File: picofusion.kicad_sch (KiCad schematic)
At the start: 48 parts, among them J1 NORTH, J2 EAST, J3 WEST, J4 SOUTH, U1 W25Q16, U2 RP2040, U3 TLV71333PDQN, U7 TJA1051TK-3, Y1 12MHz

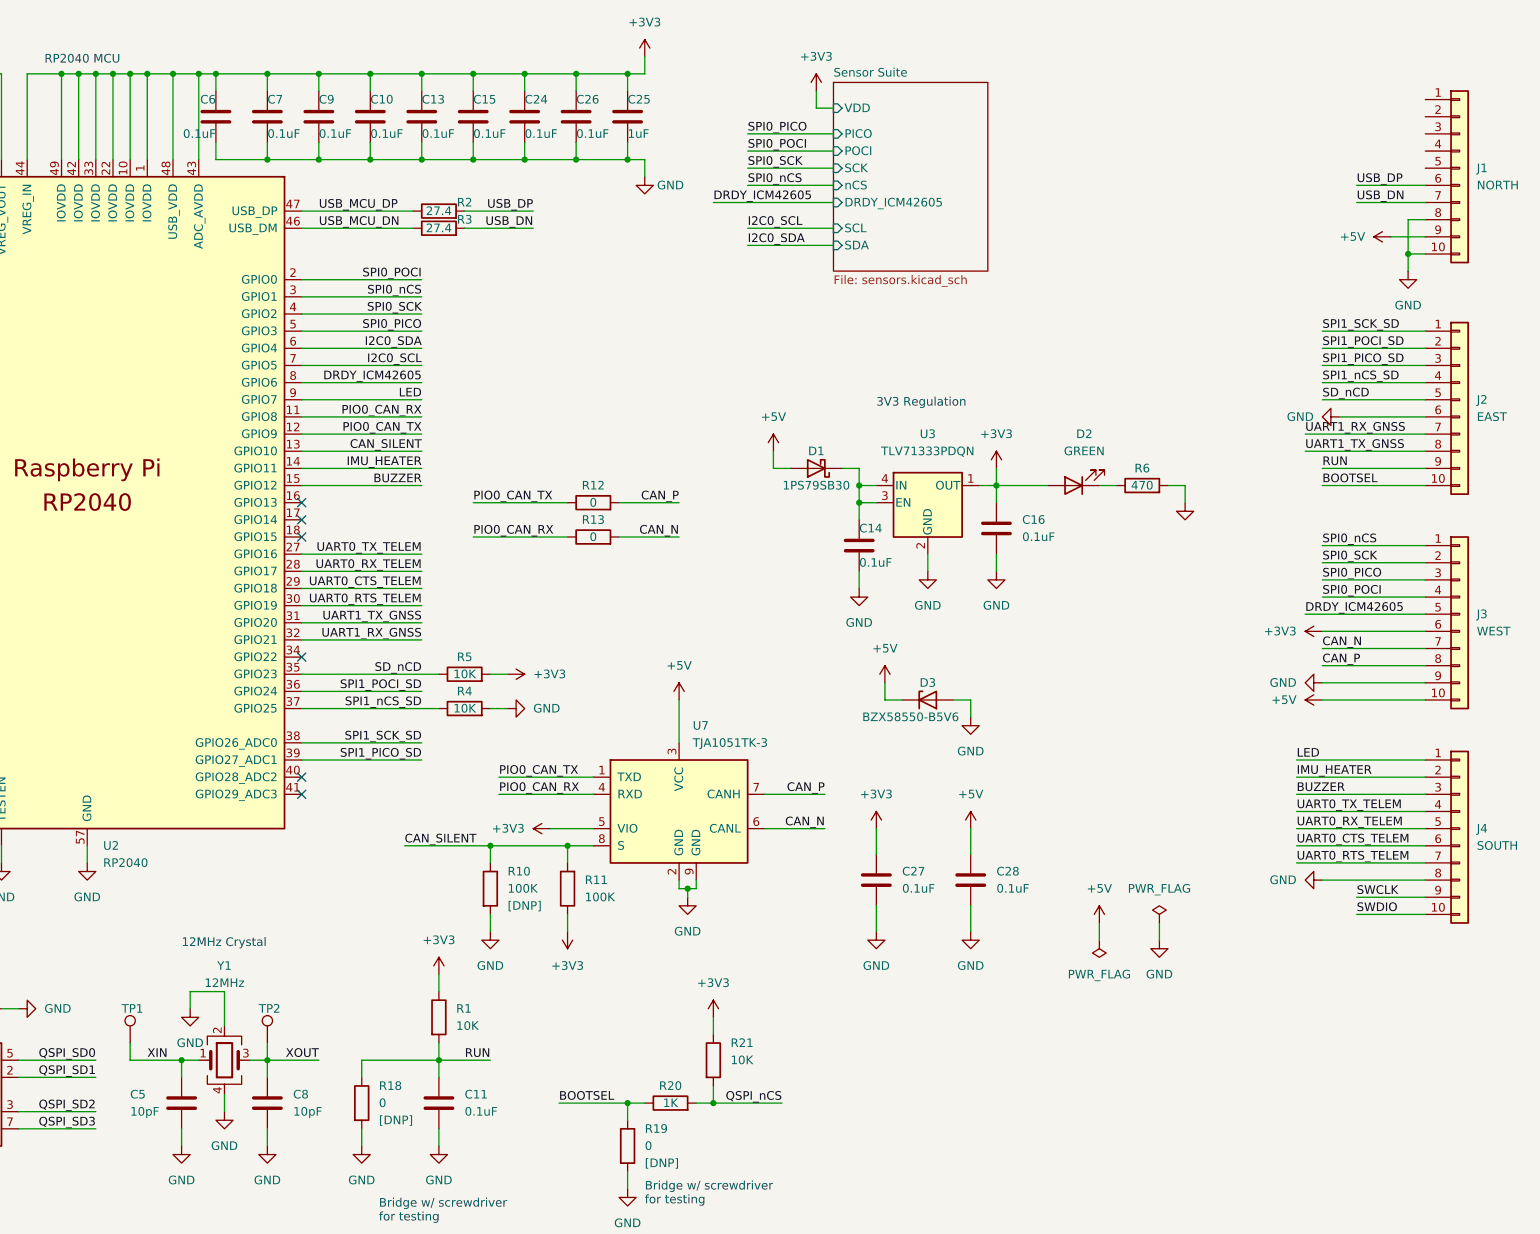
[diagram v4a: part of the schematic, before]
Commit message: h10: add graphics, fix drc, minor modifications
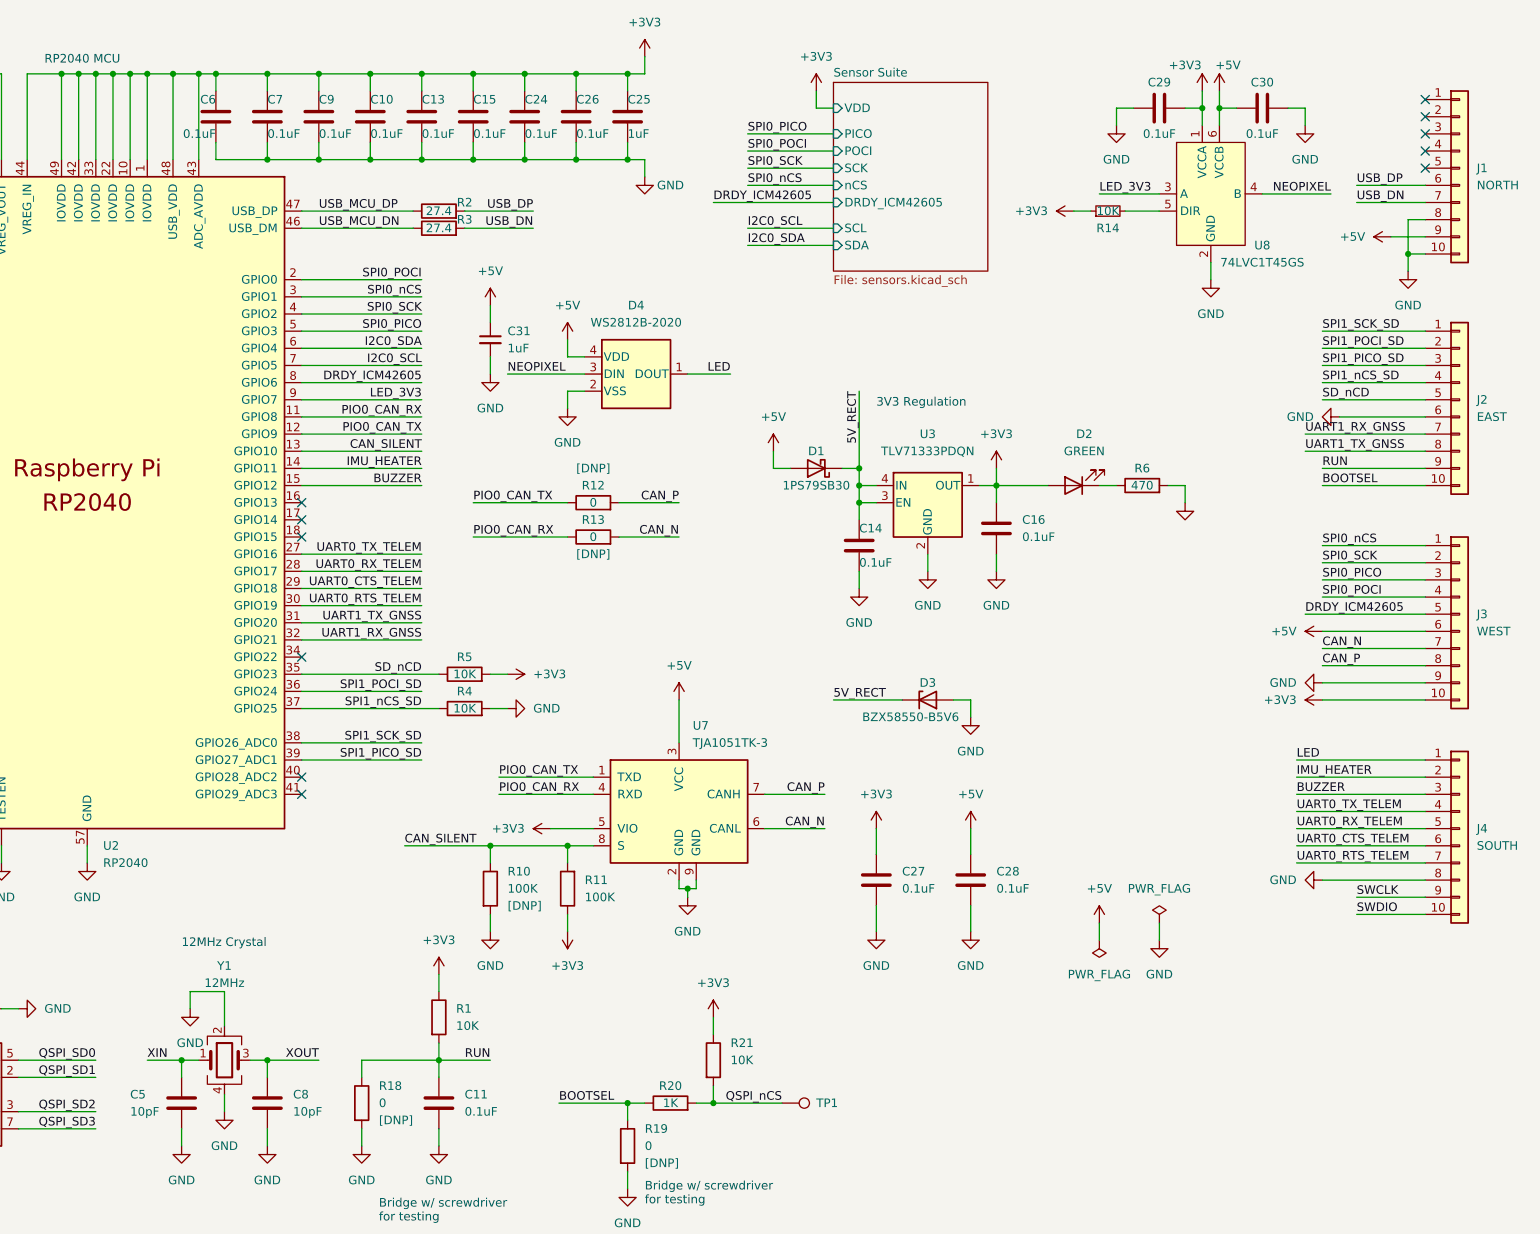
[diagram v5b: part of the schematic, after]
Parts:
- removed TP2: TestPoint, TestPoint:TestPoint_Pad_D1.0mm, symbol Connector:TestPoint
- added C29, C30: 0.1uF, Capacitor_SMD:C_0201_0603Metric, symbol Device:C
- added C31: 1uF, Capacitor_SMD:C_0201_0603Metric, symbol Device:C_Small
- added D4: WS2812B-2020, LED_SMD_Extra:WS2812B-2020, symbol LED_Extra:WS2812B-2020
- added R14: 10K, Resistor_SMD:R_0402_1005Metric, symbol Device:R_Small
- added U8: 74LVC1T45GS, 74LVC1T45:PSON35P100X100X35-6N, symbol 74LVC1T45:74LVC1T45GS
- J1, J2, J3, J4: footprint Connector_PinHeader_2.00mm:PinHeader_1x10_P2.00mm_Vertical -> picofusion_stamp:PinCastellation_1x10_P2.00mm_Vertical
- R12, R13: DNP (none) -> [DNP]
- TP1: footprint TestPoint:TestPoint_Pad_D1.0mm -> TestPoint:TestPoint_Pad_1.0x1.0mm
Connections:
- net +3V3: now also J3.10 (Pin_10), C29.2, R14.1, U8.1 (VCCA); no longer J3.6 (Pin_6)
- net +5V: now also J3.6 (Pin_6), C30.2, C31.1, D4.4 (VDD), U8.6 (VCCB); no longer D3.1 (K), J3.10 (Pin_10)
- net GND: now also C29.1, C30.1, C31.2, D4.2 (VSS), U8.2 (GND)
- net LED: now also D4.1 (DOUT); no longer U2.9 (GPIO7)
- net QSPI_nCS: now also TP1.1
- net XIN: no longer TP1.1
- net 5V_RECT: now reaches C14.1, D1.1 (K), U3.3 (EN), U3.4 (IN)
- net 5V_RECT: now also D3.1 (K)
- new net: R14.2, U8.5 (DIR)
- new net LED_3V3: U2.9 (GPIO7), U8.3 (A)
- new net NEOPIXEL: D4.3 (DIN), U8.4 (B)
- no-connect marks 6 -> 11

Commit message: h10: r2 final
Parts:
- added R15, R16, R17, R22: 22K, Resistor_SMD:R_0201_0603Metric, symbol Device:R
- C1, C10, C11, C13, C15, C2, C24, C26, C27, C28, C4, C6, C7, C9: LCSC C1525 -> (none); Mfr. # CC0201KRX5R5BB104 -> (none)
- C14, C16: LCSC C1525 -> (none)
- C25, C3: LCSC C52923 -> (none)
- C5, C8: LCSC C1547 -> (none)
- D1: LCSC C426690 -> (none)
- D2: LCSC C72043 -> (none); Part (none) -> QBLP595-IG
- J1, J2, J3, J4, TP1: now left out of the parts list
- R1, R21, R4, R5: LCSC C25744 -> (none)
- R10, R11: LCSC C25741 -> (none)
- R12, R13: LCSC C17168 -> (none)
- R2, R3: value 27.4 -> 27; LCSC C31439 -> (none)
- R6: LCSC C25117 -> (none)
- U1: LCSC C2843335 -> (none)
- U2: LCSC C2040 -> (none)
- U3: LCSC C2866431 -> (none)
- U7: LCSC C124020 -> (none)
- Y1: LCSC C521567 -> (none); Part (none) -> R2520-12.000-10-3030-TR
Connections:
- net +3V3: now also R17.1
- net +5V: now also R15.1
- net GND: now also R16.2, R22.2
- net I2C0_SCL: now also J1.4 (Pin_4)
- net I2C0_SDA: now also J1.5 (Pin_5)
- net RESV1: now reaches U2.16 (GPIO13)
- net RESV1: now also J1.3 (Pin_3)
- net 3V3_SENSE: now reaches U2.40 (GPIO28_ADC2)
- net 3V3_SENSE: now also R17.2, R22.1
- net 5V_SENSE: now reaches U2.41 (GPIO29_ADC3)
- net 5V_SENSE: now also R15.2, R16.1
- no-connect marks 11 -> 5
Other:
- moved on the sheet: C27, C28

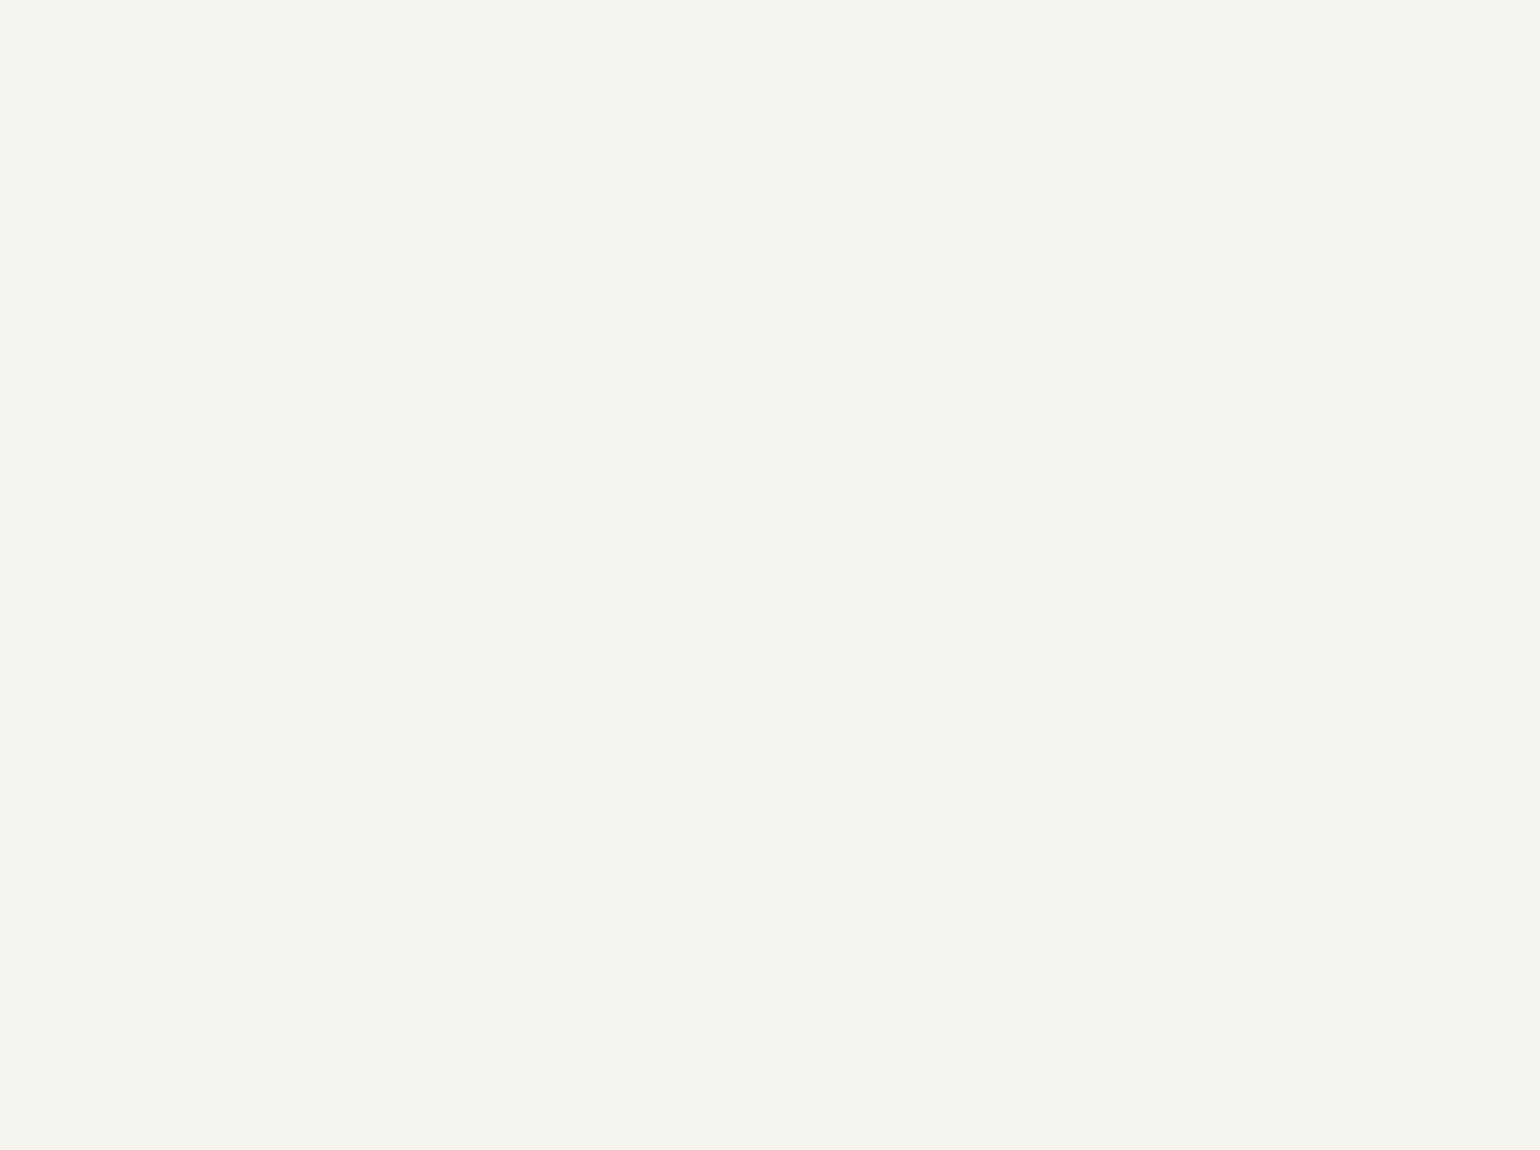
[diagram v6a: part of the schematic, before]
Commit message: added f412 and did test routing
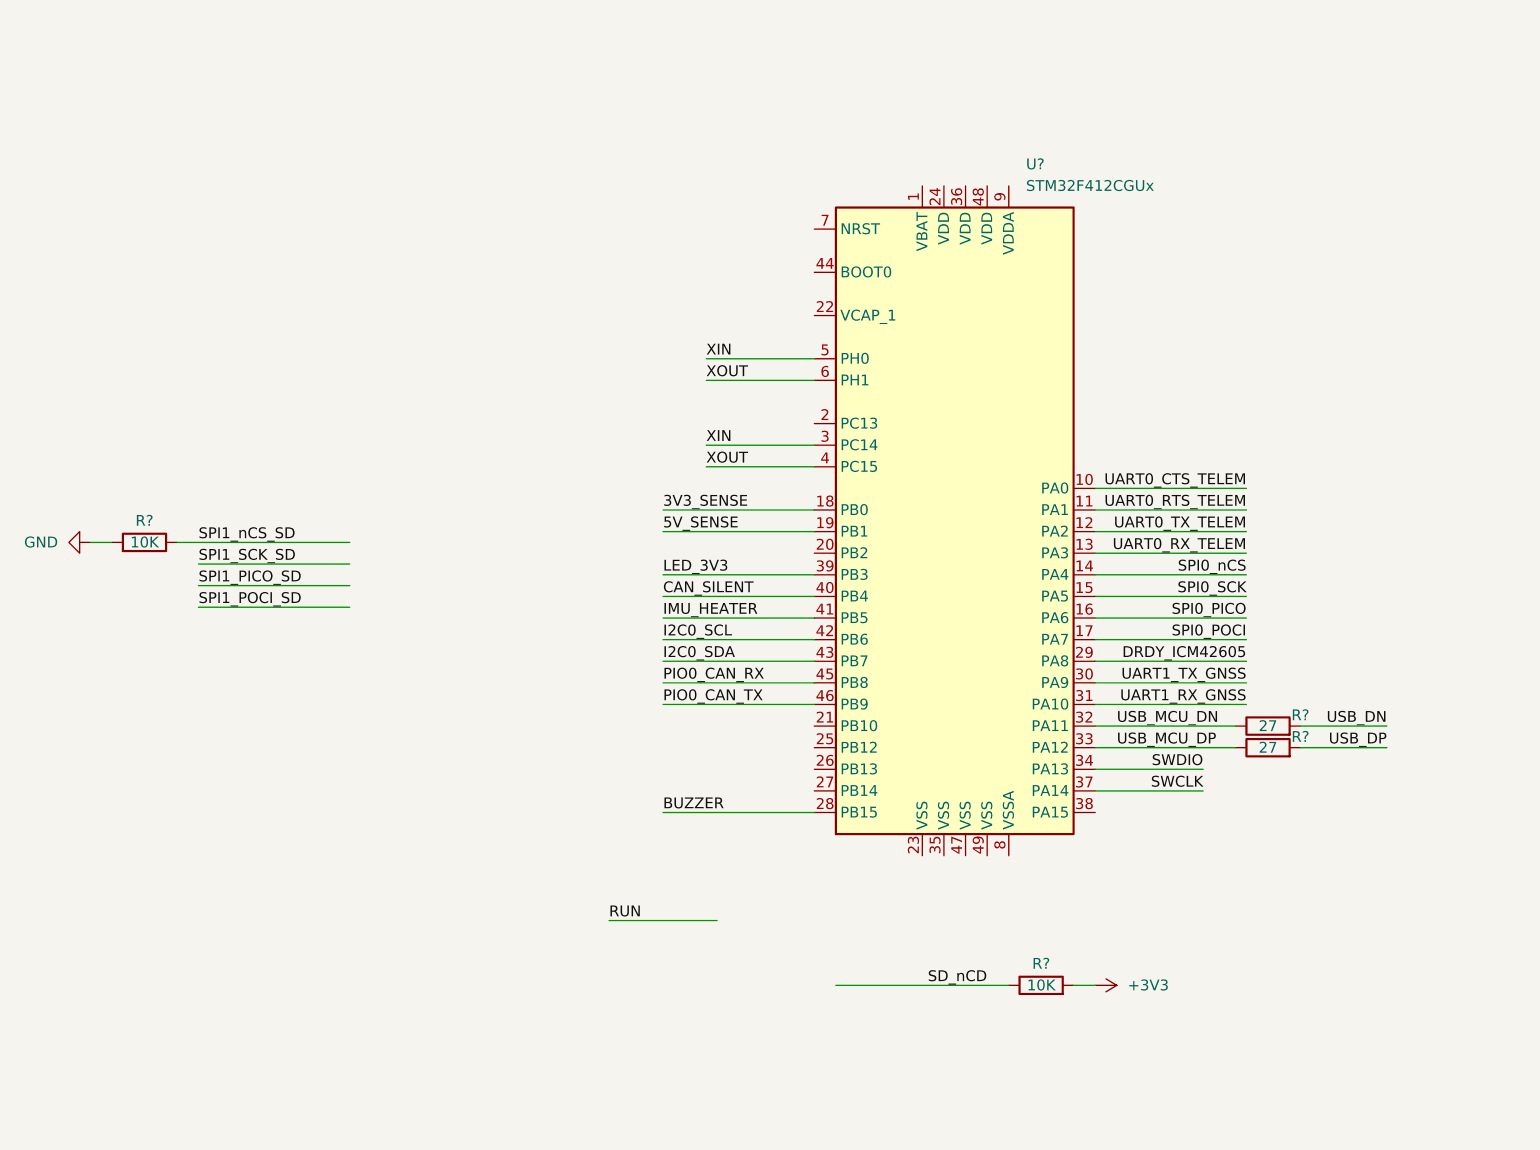
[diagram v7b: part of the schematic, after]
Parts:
- added R? (x2): 27, Resistor_SMD:R_0201_0603Metric, symbol Device:R
- added R? (x2): 10K, Resistor_SMD:R_0402_1005Metric, symbol Device:R
- added U?: STM32F412CGUx, Package_DFN_QFN:QFN-48-1EP_7x7mm_P0.5mm_EP5.6x5.6mm, symbol MCU_ST_STM32F4:STM32F412CGUx
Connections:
- net +3V3: now also R?.2
- net 3V3_SENSE: now also U?.18 (PB0)
- net 5V_SENSE: now also U?.19 (PB1)
- net BUZZER: now also U?.28 (PB15)
- net CAN_SILENT: now also U?.40 (PB4)
- net DRDY_ICM42605: now also U?.29 (PA8)
- net GND: now also R?.2
- net I2C0_SCL: now also U?.42 (PB6)
- net I2C0_SDA: now also U?.43 (PB7)
- net IMU_HEATER: now also U?.41 (PB5)
- net LED_3V3: now also U?.39 (PB3)
- net PIO0_CAN_RX: now also U?.45 (PB8)
- net PIO0_CAN_TX: now also U?.46 (PB9)
- net SD_nCD: now also R?.1
- net SPI0_PICO: now also U?.16 (PA6)
- net SPI0_POCI: now also U?.17 (PA7)
- net SPI0_SCK: now also U?.15 (PA5)
- net SPI0_nCS: now also U?.14 (PA4)
- net SPI1_nCS_SD: now also R?.1
- net SWCLK: now also U?.37 (PA14)
- net SWDIO: now also U?.34 (PA13)
- net UART0_CTS_TELEM: now also U?.10 (PA0)
- net UART0_RTS_TELEM: now also U?.11 (PA1)
- net UART0_RX_TELEM: now also U?.13 (PA3)
- net UART0_TX_TELEM: now also U?.12 (PA2)
- net UART1_RX_GNSS: now also U?.31 (PA10)
- net UART1_TX_GNSS: now also U?.30 (PA9)
- net USB_DN: now also R?.2
- net USB_DP: now also R?.2
- net USB_MCU_DN: now also R?.1, U?.32 (PA11)
- net USB_MCU_DP: now also R?.1, U?.33 (PA12)
- net XIN: now also U?.3 (PC14), U?.5 (PH0)
- net XOUT: now also U?.4 (PC15), U?.6 (PH1)
